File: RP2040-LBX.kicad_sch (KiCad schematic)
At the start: 42 parts, among them J1 USB C Connector, J2 JTAG_TC2030, SW1 Boot, U1 XC6206, U2 USBLC6-2SC6, U3 RP2040, U4 W25Q128JVS, Y1 12MHz

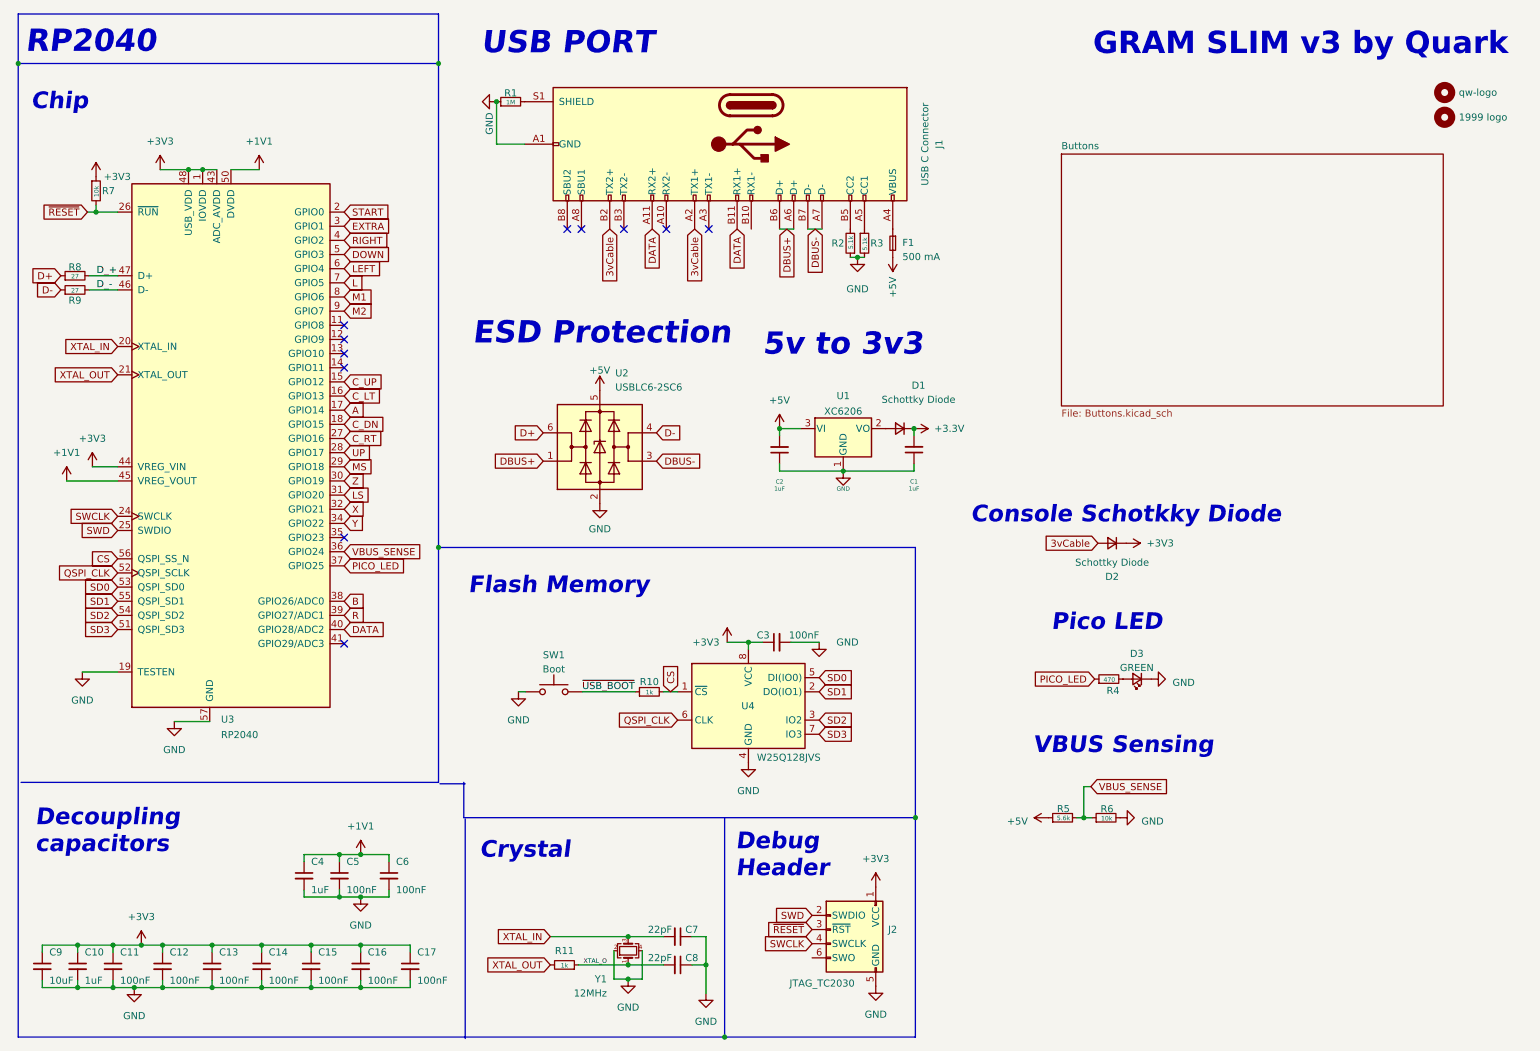
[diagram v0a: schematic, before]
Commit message: feat: add tactile switches to lbx
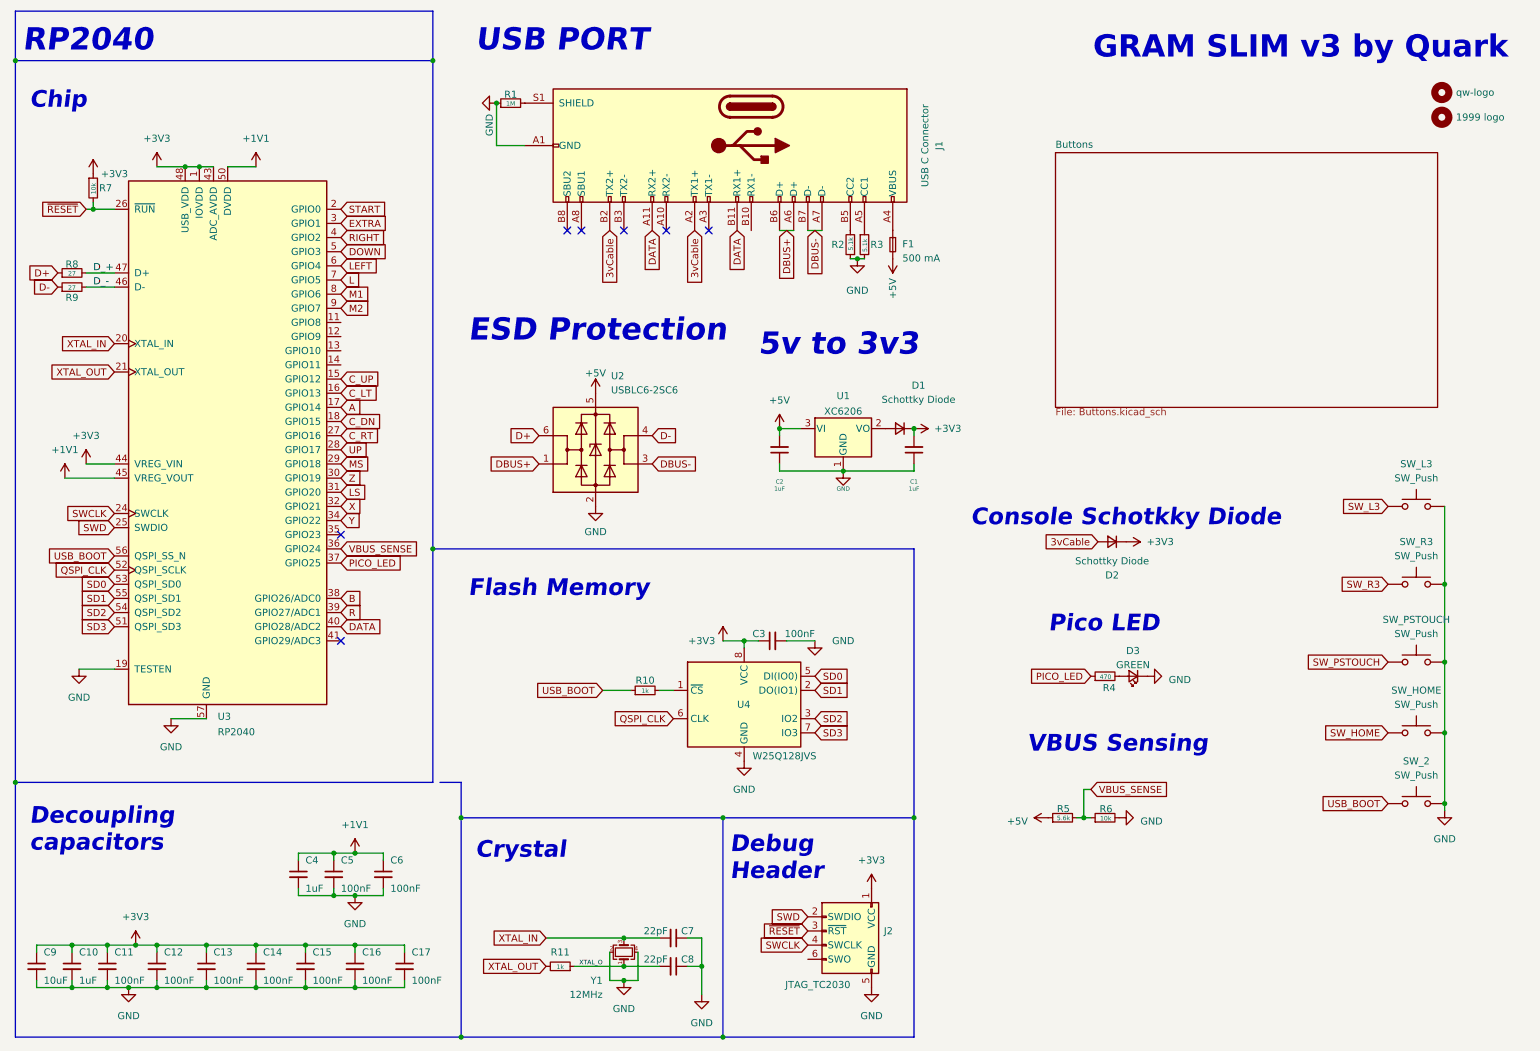
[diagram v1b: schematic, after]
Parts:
- removed SW1: Boot, Button_Switch_SMD:SW_SPST_SKQG_WithStem, symbol Switch:SW_Push
- added SW_2, SW_HOME, SW_L3, SW_PSTOUCH, SW_R3: SW_Push, symbol Switch:SW_Push
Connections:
- net GND: now also SW_2.2, SW_HOME.2, SW_L3.2, SW_PSTOUCH.2, SW_R3.2
- net CS: no longer names the net of R10.2, U4.1 (~{CS})
- net CS: no longer U3.56 (QSPI_SS_N)
- net ~{USB_BOOT} renamed USB_BOOT
- net USB_BOOT: now also U3.56 (QSPI_SS_N), SW_2.1
- new net SW_HOME: SW_HOME.1
- new net SW_L3: SW_L3.1
- new net SW_PSTOUCH: SW_PSTOUCH.1
- new net SW_R3: SW_R3.1
- no-connect marks 11 -> 7
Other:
- moved on the sheet: C10, C11, C12, C13, C14, C15, C16, C17, C3, C4, C5, C6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

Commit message: assign footprints to the push buttons
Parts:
- SW_BOOTSEL1: renamed from SW_2; footprint (none) -> ul_TS-1187A-B-A-B:TS-1187A-B-A-B_XKB
- SW_HOME1: renamed from SW_HOME; footprint (none) -> ul_TS-1187A-B-A-B:TS-1187A-B-A-B_XKB
- SW_L3, SW_R3: footprint (none) -> ul_TS-1187A-B-A-B:TS-1187A-B-A-B_XKB
- SW_PSTOUCH1: renamed from SW_PSTOUCH; footprint (none) -> ul_TS-1187A-B-A-B:TS-1187A-B-A-B_XKB
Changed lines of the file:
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@@
 		(dnp no)
 		(fields_autoplaced yes)
-		(property "Reference" "SW_2"
+		(property "Reference" "SW_BOOTSEL1"
 			(at 264.16 147.32 0)
 			(show_name no)
@@
 			)
 		)
-		(property "Footprint" ""
+		(property "Footprint" "ul_TS-1187A-B-A-B:TS-1187A-B-A-B_XKB"
 			(at 264.16 149.86 0)
 			(hide yes)
@@
 			(project "RP2040-LBX"
 				(path "/17c378e5-d065-46dd-aa4a-654e3a402061"
-					(reference "SW_2")
+					(reference "SW_BOOTSEL1")
 					(unit 1)
 				)
@@
 			)
 		)
-		(property "Footprint" ""
+		(property "Footprint" "ul_TS-1187A-B-A-B:TS-1187A-B-A-B_XKB"
 			(at 264.16 110.49 0)
 			(hide yes)
@@
 			)
 		)
-		(property "Footprint" ""
+		(property "Footprint" "ul_TS-1187A-B-A-B:TS-1187A-B-A-B_XKB"
 			(at 264.16 96.52 0)
 			(hide yes)
@@
 		(dnp no)
 		(fields_autoplaced yes)
-		(property "Reference" "SW_PSTOUCH"
+		(property "Reference" "SW_PSTOUCH1"
 			(at 264.16 121.92 0)
 			(show_name no)
@@
 			)
 		)
-		(property "Footprint" ""
+		(property "Footprint" "ul_TS-1187A-B-A-B:TS-1187A-B-A-B_XKB"
 			(at 264.16 124.46 0)
 			(hide yes)
@@
 			(project "RP2040-LBX"
 				(path "/17c378e5-d065-46dd-aa4a-654e3a402061"
-					(reference "SW_PSTOUCH")
+					(reference "SW_PSTOUCH1")
 					(unit 1)
 				)
@@
 		(dnp no)
 		(fields_autoplaced yes)
-		(property "Reference" "SW_HOME"
+		(property "Reference" "SW_HOME1"
 			(at 264.16 134.62 0)
 			(show_name no)
@@
 			)
 		)
-		(property "Footprint" ""
+		(property "Footprint" "ul_TS-1187A-B-A-B:TS-1187A-B-A-B_XKB"
 			(at 264.16 137.16 0)
 			(hide yes)
@@
 			(project "RP2040-LBX"
 				(path "/17c378e5-d065-46dd-aa4a-654e3a402061"
-					(reference "SW_HOME")
+					(reference "SW_HOME1")
 					(unit 1)
 				)

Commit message: add part numbers
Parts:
- SW_BOOTSEL1, SW_HOME1, SW_L3, SW_PSTOUCH1, SW_R3: LCSC (none) -> C318886
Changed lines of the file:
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@@
 			)
 		)
+		(property "LCSC" "C318886"
+			(at 264.16 154.94 0)
+			(hide yes)
+			(show_name no)
+			(do_not_autoplace no)
+			(effects
+				(font
+					(size 1.27 1.27)
+				)
+			)
+		)
 		(pin "2"
 		)
@@
 			)
 		)
+		(property "LCSC" "C318886"
+			(at 264.16 115.57 0)
+			(hide yes)
+			(show_name no)
+			(do_not_autoplace no)
+			(effects
+				(font
+					(size 1.27 1.27)
+				)
+			)
+		)
 		(pin "2"
 		)
@@
 			)
 		)
+		(property "LCSC" "C318886"
+			(at 264.16 101.6 0)
+			(hide yes)
+			(show_name no)
+			(do_not_autoplace no)
+			(effects
+				(font
+					(size 1.27 1.27)
+				)
+			)
+		)
 		(pin "2"
 		)
@@
 			)
 		)
+		(property "LCSC" "C318886"
+			(at 264.16 129.54 0)
+			(hide yes)
+			(show_name no)
+			(do_not_autoplace no)
+			(effects
+				(font
+					(size 1.27 1.27)
+				)
+			)
+		)
 		(pin "2"
 		)
@@
 			(at 264.16 142.24 0)
 			(hide yes)
+			(show_name no)
+			(do_not_autoplace no)
+			(effects
+				(font
+					(size 1.27 1.27)
+				)
+			)
+		)
+		(property "LCSC" "C318886"
+			(at 264.16 142.24 0)
+			(hide yes)

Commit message: Add missing LCSC values to board
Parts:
- D3: LCSC (none) -> C2297
- F1: LCSC (none) -> C2836286
- R4: LCSC (none) -> C25117
- R5: LCSC (none) -> C23189
- R6: LCSC (none) -> C25804
- U2: LCSC (none) -> C2827654
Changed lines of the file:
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@@
 			)
 		)
+		(property "LCSC" "C2297"
+			(at 213.36 132.08 90)
+			(hide yes)
+			(show_name no)
+			(do_not_autoplace no)
+			(effects
+				(font
+					(size 1.27 1.27)
+				)
+			)
+		)
 		(property "Datasheet" ""
 			(at 213.36 132.08 90)
@@
 			)
 		)
+		(property "LCSC" "C25804"
+			(at 208.28 157.48 0)
+			(hide yes)
+			(show_name no)
+			(do_not_autoplace no)
+			(effects
+				(font
+					(size 1.27 1.27)
+				)
+			)
+		)
 		(property "Datasheet" ""
 			(at 208.28 157.48 0)
@@
 			)
 		)
+		(property "LCSC" "C25117"
+			(at 208.28 132.08 0)
+			(hide yes)
+			(show_name no)
+			(do_not_autoplace no)
+			(effects
+				(font
+					(size 1.27 1.27)
+				)
+			)
+		)
 		(property "Datasheet" ""
 			(at 208.28 132.08 0)
@@
 			)
 		)
+		(property "LCSC" "C2836286"
+			(at 170.18 54.61 0)
+			(hide yes)
+			(show_name no)
+			(do_not_autoplace no)
+			(effects
+				(font
+					(size 1.27 1.27)
+				)
+			)
+		)
 		(property "Datasheet" ""
 			(at 170.18 54.61 0)
@@
 			)
 		)
+		(property "LCSC" "C2827654"
+			(at 116.84 104.14 0)
+			(hide yes)
+			(show_name no)
+			(do_not_autoplace no)
+			(effects
+				(font
+					(size 1.27 1.27)
+				)
+			)
+		)
 		(property "Datasheet" "https://www.st.com/resource/en/datasheet/usblc6-2.pdf"
 			(at 121.92 82.55 0)
@@
 			(at 200.66 157.48 0)
 			(hide yes)
+			(show_name no)
+			(do_not_autoplace no)
+			(effects
+				(font
+					(size 1.27 1.27)
+				)
+			)
+		)
+		(property "LCSC" "C23189"
+			(at 200.66 157.48 0)
+			(hide yes)

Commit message: Update R1/R2/R3 LCSC values using IntegratedOF1 as source of truth
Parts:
- R1: LCSC C25190 -> C22935
- R2, R3: LCSC C25744 -> C25905
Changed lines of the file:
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@@
 			)
 		)
-		(property "LCSC" "C25190"
+		(property "LCSC" "C22935"
 			(at 101.6 29.21 0)
 			(hide yes)
@@
 			)
 		)
-		(property "LCSC" "C25744"
+		(property "LCSC" "C25905"
 			(at 165.1 54.61 0)
 			(hide yes)
@@
 			)
 		)
-		(property "LCSC" "C25744"
+		(property "LCSC" "C25905"
 			(at 162.56 54.61 0)
 			(hide yes)

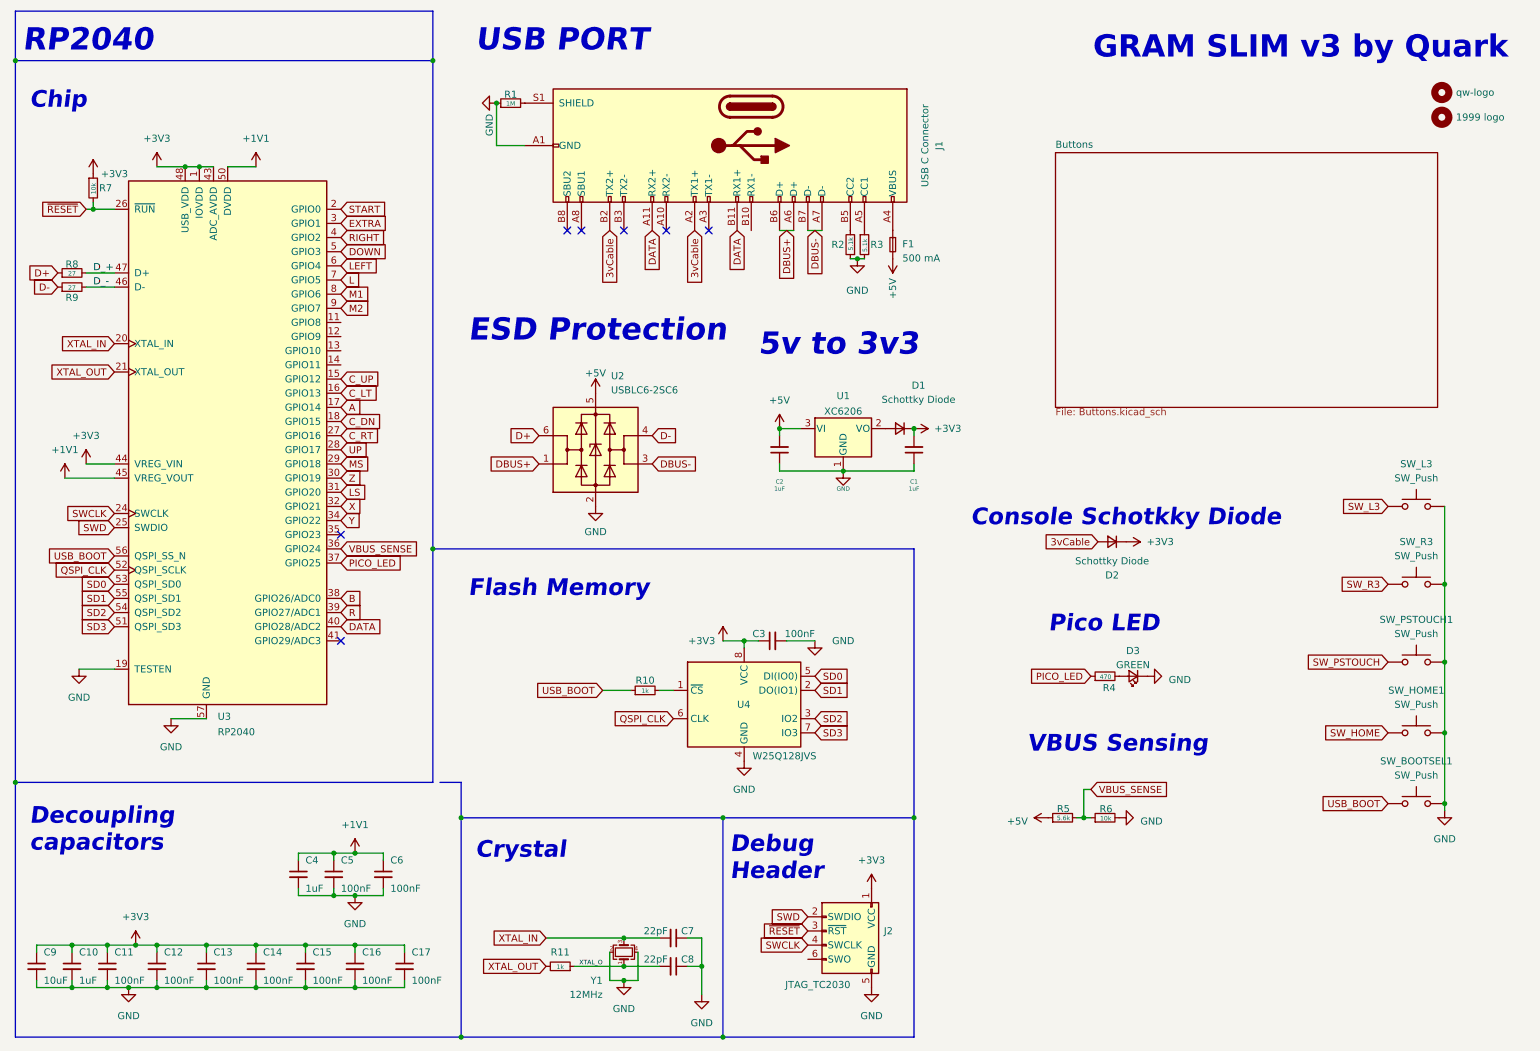
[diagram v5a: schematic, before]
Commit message: place and route extra switches
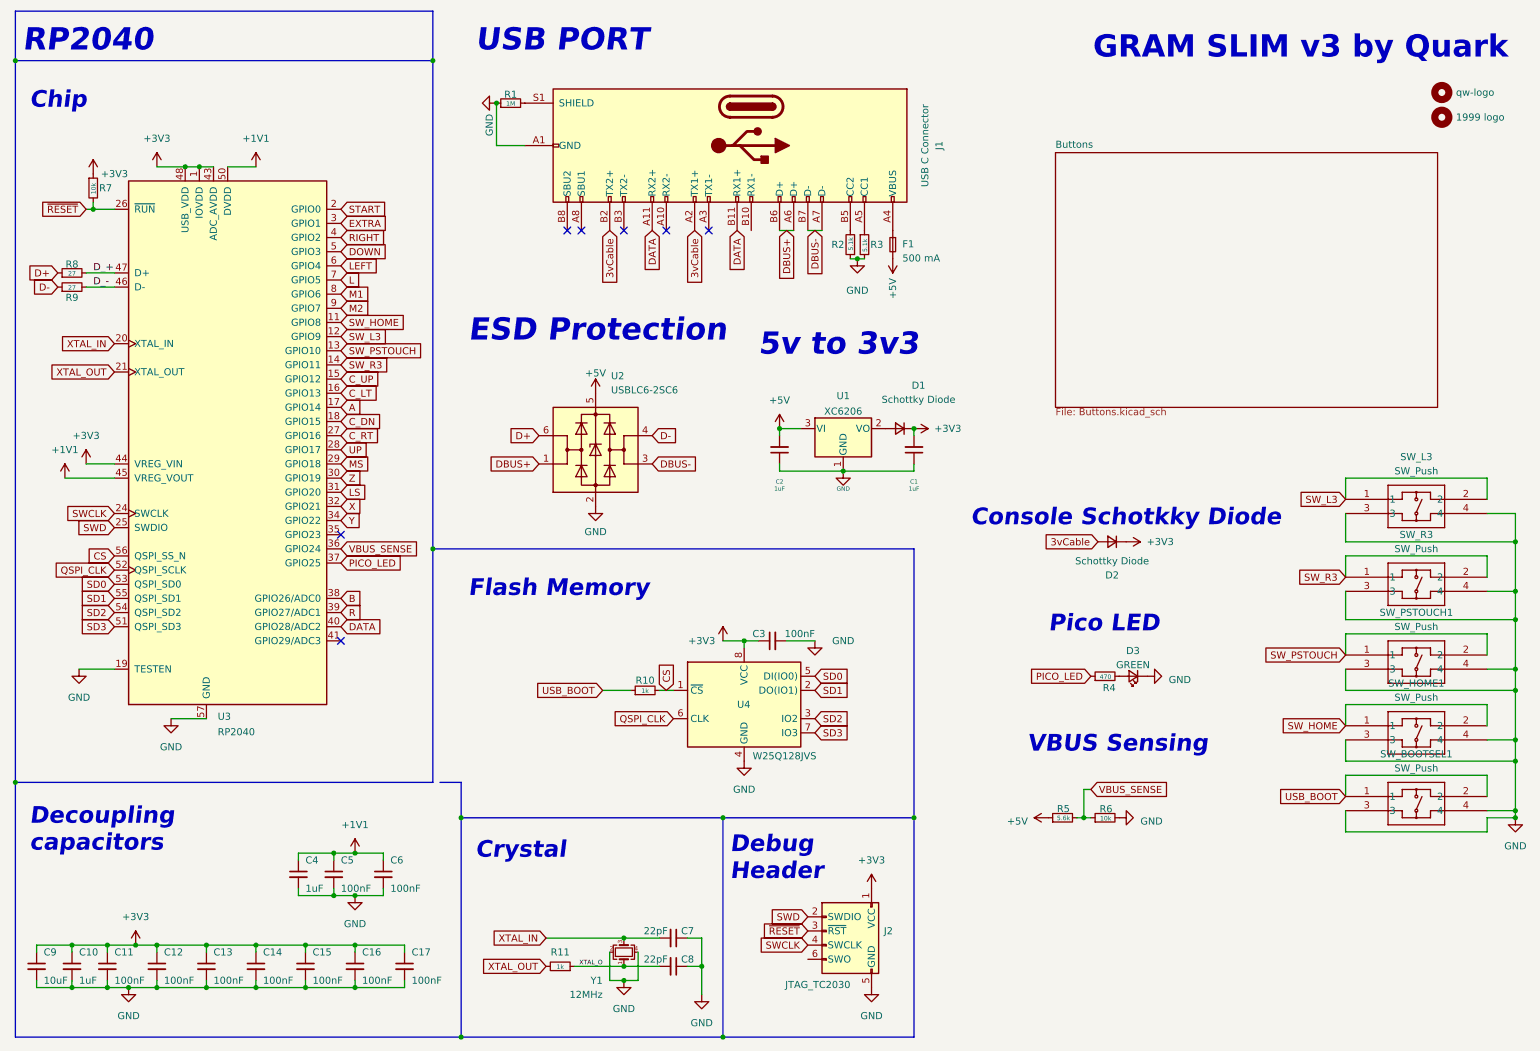
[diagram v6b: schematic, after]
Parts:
- SW_BOOTSEL1, SW_HOME1, SW_L3, SW_PSTOUCH1, SW_R3: footprint ul_TS-1187A-B-A-B:TS-1187A-B-A-B_XKB -> TS-1187A-B-A-B_XKB; symbol Switch:SW_Push -> 2026-04-12_20-29-11:TS-1187A-B-A-B
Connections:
- net GND: now also SW_BOOTSEL1.3, SW_BOOTSEL1.4, SW_HOME1.3, SW_HOME1.4, SW_L3.3, SW_L3.4, SW_PSTOUCH1.3, SW_PSTOUCH1.4, SW_R3.3, SW_R3.4; no longer SW_BOOTSEL1.2, SW_HOME1.2, SW_L3.2, SW_PSTOUCH1.2, SW_R3.2
- net SW_HOME: now also SW_HOME1.2, U3.11 (GPIO8)
- net SW_L3: now also SW_L3.2, U3.12 (GPIO9)
- net SW_PSTOUCH: now also SW_PSTOUCH1.2, U3.13 (GPIO10)
- net SW_R3: now also SW_R3.2, U3.14 (GPIO11)
- net USB_BOOT: now also SW_BOOTSEL1.2; no longer U3.56 (QSPI_SS_N)
- net CS: now reaches R10.2, U4.1 (~{CS})
- net CS: now also U3.56 (QSPI_SS_N)
